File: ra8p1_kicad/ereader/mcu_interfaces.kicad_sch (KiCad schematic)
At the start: 8 parts, among them U1 R7KA8P1KFLCAC#UC0

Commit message: Wire e-reader user controls and record power architecture
Connect four protected page/volume inputs and power INT/KILL interfaces through the native hierarchy. Include exact sourcing, linked calculations, local symbols, expanded requirements, and a fresh eight-page PDF and full BOM.

Progress checkpoint, not fabrication release: power source, EN supervision and discharge remain unfinished. Configured ERC: 204 errors and 2 warnings, versus 208 and 2 at the previous checkpoint; six MCU disconnections resolved and two explicit power-draft gaps added. Page/volume sheet has zero findings. One independent review round: no findings. Arithmetic, netlist/BOM consistency and all PDF pages reviewed. Hardware-only hook bypass explicitly authorized.
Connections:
- net PAGE_PREV_N: now reaches U1.A12 (P309)
- net VOL_DOWN_N: now reaches U1.B12 (P311)
- net POWER_BUTTON_N: now reaches U1.B6 (P303)
- net PAGE_NEXT_N: now reaches U1.E10 (P310)
- net VOL_UP_N: now reaches U1.B14 (P909)
- net POWER_KILL_N: now reaches U1.D9 (P903)
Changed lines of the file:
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@@
 	(wire
 		(pts
+			(xy 264.16 76.2) (xy 279.4 76.2)
+		)
+		(stroke
+			(width 0)
+			(type default)
+		)
+	)
+	(wire
+		(pts
 			(xy 20.32 220.98) (xy 30.48 220.98)
 		)
@@
 	(wire
 		(pts
+			(xy 167.64 139.7) (xy 182.88 139.7)
+		)
+		(stroke
+			(width 0)
+			(type default)
+		)
+	)
+	(wire
+		(pts
+			(xy 264.16 55.88) (xy 279.4 55.88)
+		)
+		(stroke
+			(width 0)
+			(type default)
+		)
+	)
+	(wire
+		(pts
 			(xy 266.7 213.36) (xy 304.8 213.36)
 		)
@@
 	(wire
 		(pts
+			(xy 264.16 71.12) (xy 279.4 71.12)
+		)
+		(stroke
+			(width 0)
+			(type default)
+		)
+	)
+	(wire
+		(pts
 			(xy 71.12 124.46) (xy 96.52 124.46)
 		)
@@
 	(wire
 		(pts
+			(xy 167.64 124.46) (xy 182.88 124.46)
+		)
+		(stroke
+			(width 0)
+			(type default)
+		)
+	)
+	(wire
+		(pts
 			(xy 71.12 137.16) (xy 96.52 137.16)
 		)
@@
 	(wire
 		(pts
+			(xy 264.16 73.66) (xy 279.4 73.66)
+		)
+		(stroke
+			(width 0)
+			(type default)
+		)
+	)
+	(wire
+		(pts
 			(xy 71.12 121.92) (xy 96.52 121.92)
 		)
@@
 		)
 	)
+	(hierarchical_label "VOL_UP_N"
+		(shape input)
+		(at 182.88 139.7 0)
+		(effects
+			(font
+				(size 1.27 1.27)
+			)
+			(justify left)
+		)
+	)
 	(hierarchical_label "RADIO_DATA_READY"
 		(shape input)
@@
 		)
 	)
+	(hierarchical_label "POWER_BUTTON_N"
+		(shape input)
+		(at 279.4 55.88 0)
+		(effects
+			(font
+				(size 1.27 1.27)
+			)
+			(justify left)
+		)
+	)
+	(hierarchical_label "PAGE_PREV_N"
+		(shape input)
+		(at 279.4 71.12 0)
+		(effects
+			(font
+				(size 1.27 1.27)
+			)
+			(justify left)
+		)
+	)
+	(hierarchical_label "POWER_KILL_N"
+		(shape output)
+		(at 182.88 124.46 0)
+		(effects
+			(font
+				(size 1.27 1.27)
+			)
+			(justify left)
+		)
+	)
+	(hierarchical_label "VOL_DOWN_N"
+		(shape input)
+		(at 279.4 76.2 0)
+		(effects
+			(font
+				(size 1.27 1.27)
+			)
+			(justify left)
+		)
+	)
 	(hierarchical_label "RADIO_SCLK"
 		(shape output)
@@
 		)
 	)
+	(hierarchical_label "PAGE_NEXT_N"
+		(shape input)
+		(at 279.4 73.66 0)
+		(effects
+			(font
+				(size 1.27 1.27)
+			)
+			(justify left)
+		)
+	)
 	(symbol
 		(lib_id "power:+3V3")
@@
 		)
 		(pin "E10"
+			(alternate "P310_IN")
 		)
 		(pin "F14"
@@
 		)
 		(pin "B14"
+			(alternate "P909_IN")
 		)
 		(pin "C12"
 		)
 		(pin "D9"
+			(alternate "P903_OD")
 		)
 		(pin "D12"
@@
 		)
 		(pin "A12"
+			(alternate "P309_IN")
 		)
 		(pin "A17"
@@
 		)
 		(pin "B6"
+			(alternate "P303_IN")
 		)
 		(pin "B12"
+			(alternate "P311_IN")
 		)
 		(pin "B15"
@@
 		)
 		(pin "B6"
+			(alternate "P303_IN")
 		)
 		(pin "D10"
@@
 		)
 		(pin "A12"
+			(alternate "P309_IN")
 		)
 		(pin "E10"
+			(alternate "P310_IN")
 		)
 		(pin "B12"
+			(alternate "P311_IN")
 		)
 		(pin "C13"
@@
 		)
 		(pin "B14"
+			(alternate "P909_IN")
 		)
 		(pin "C12"
 		)
 		(pin "D9"
+			(alternate "P903_OD")
 		)
 		(pin "E11"
@@
 		)
 		(pin "D9"
+			(alternate "P903_OD")
 		)
 		(pin "J3"
@@
 		)
 		(pin "E10"
+			(alternate "P310_IN")
 		)
 		(pin "D11"
@@
 		)
 		(pin "A12"
+			(alternate "P309_IN")
 		)
 		(pin "A17"
@@
 		)
 		(pin "B6"
+			(alternate "P303_IN")
 		)
 		(pin "B12"
+			(alternate "P311_IN")
 		)
 		(pin "B15"
@@
 		)
 		(pin "B14"
+			(alternate "P909_IN")
 		)
 		(pin "C12"
@@
 		)
 		(pin "D9"
+			(alternate "P903_OD")
 		)
 		(pin "A16"
@@
 		)
 		(pin "B14"
+			(alternate "P909_IN")
 		)
 		(pin "E11"
@@
 		)
 		(pin "A12"
+			(alternate "P309_IN")
 		)
 		(pin "A17"
@@
 		)
 		(pin "B6"
+			(alternate "P303_IN")
 		)
 		(pin "B12"
+			(alternate "P311_IN")
 		)
 		(pin "B15"
@@
 		)
 		(pin "E10"
+			(alternate "P310_IN")
 		)
 		(pin "F14"
@@
 		)
 		(pin "A12"
+			(alternate "P309_IN")
 		)
 		(pin "A17"
@@
 		)
 		(pin "B6"
+			(alternate "P303_IN")
 		)
 		(pin "B12"
+			(alternate "P311_IN")
 		)
 		(pin "B15"
@@
 		)
 		(pin "E10"
+			(alternate "P310_IN")
 		)
 		(pin "F14"
@@
 		)
 		(pin "B14"
+			(alternate "P909_IN")
 		)
 		(pin "C12"
 		)
 		(pin "D9"
+			(alternate "P903_OD")
 		)
 		(pin "D12"
@@
 		)
 		(pin "B14"
+			(alternate "P909_IN")
 		)
 		(pin "C12"
@@
 		)
 		(pin "D9"
+			(alternate "P903_OD")
 		)
 		(pin "U5"
@@
 		)
 		(pin "A12"
+			(alternate "P309_IN")
 		)
 		(pin "A17"
@@
 		)
 		(pin "E10"
+			(alternate "P310_IN")
 		)
 		(pin "D11"
@@
 		)
 		(pin "B6"
+			(alternate "P303_IN")
 		)
 		(pin "B12"
+			(alternate "P311_IN")
 		)
 		(pin "C10"
@@
 		)
 		(pin "A12"
+			(alternate "P309_IN")
 		)
 		(pin "A5"
@@
 		)
 		(pin "D9"
+			(alternate "P903_OD")
 		)
 		(pin "C12"
 		)
 		(pin "B14"
+			(alternate "P909_IN")
 		)
 		(pin "B13"
@@
 		)
 		(pin "E10"
+			(alternate "P310_IN")
 		)
 		(pin "D11"
@@
 		)
 		(pin "B6"
+			(alternate "P303_IN")
 		)
 		(pin "B5"
@@
 		)
 		(pin "B12"
+			(alternate "P311_IN")
 		)
 		(pin "C11"
@@
 		)
 		(pin "B14"
+			(alternate "P909_IN")
 		)
 		(pin "C12"
 		)
 		(pin "D9"
+			(alternate "P903_OD")
 		)
 		(pin "D12"
@@
 		)
 		(pin "E10"
+			(alternate "P310_IN")
 		)
 		(pin "F14"
@@
 		)
 		(pin "A12"
+			(alternate "P309_IN")
 		)
 		(pin "A17"
@@
 		)
 		(pin "B6"
+			(alternate "P303_IN")
 		)
 		(pin "B12"
+			(alternate "P311_IN")
 		)
 		(pin "B15"

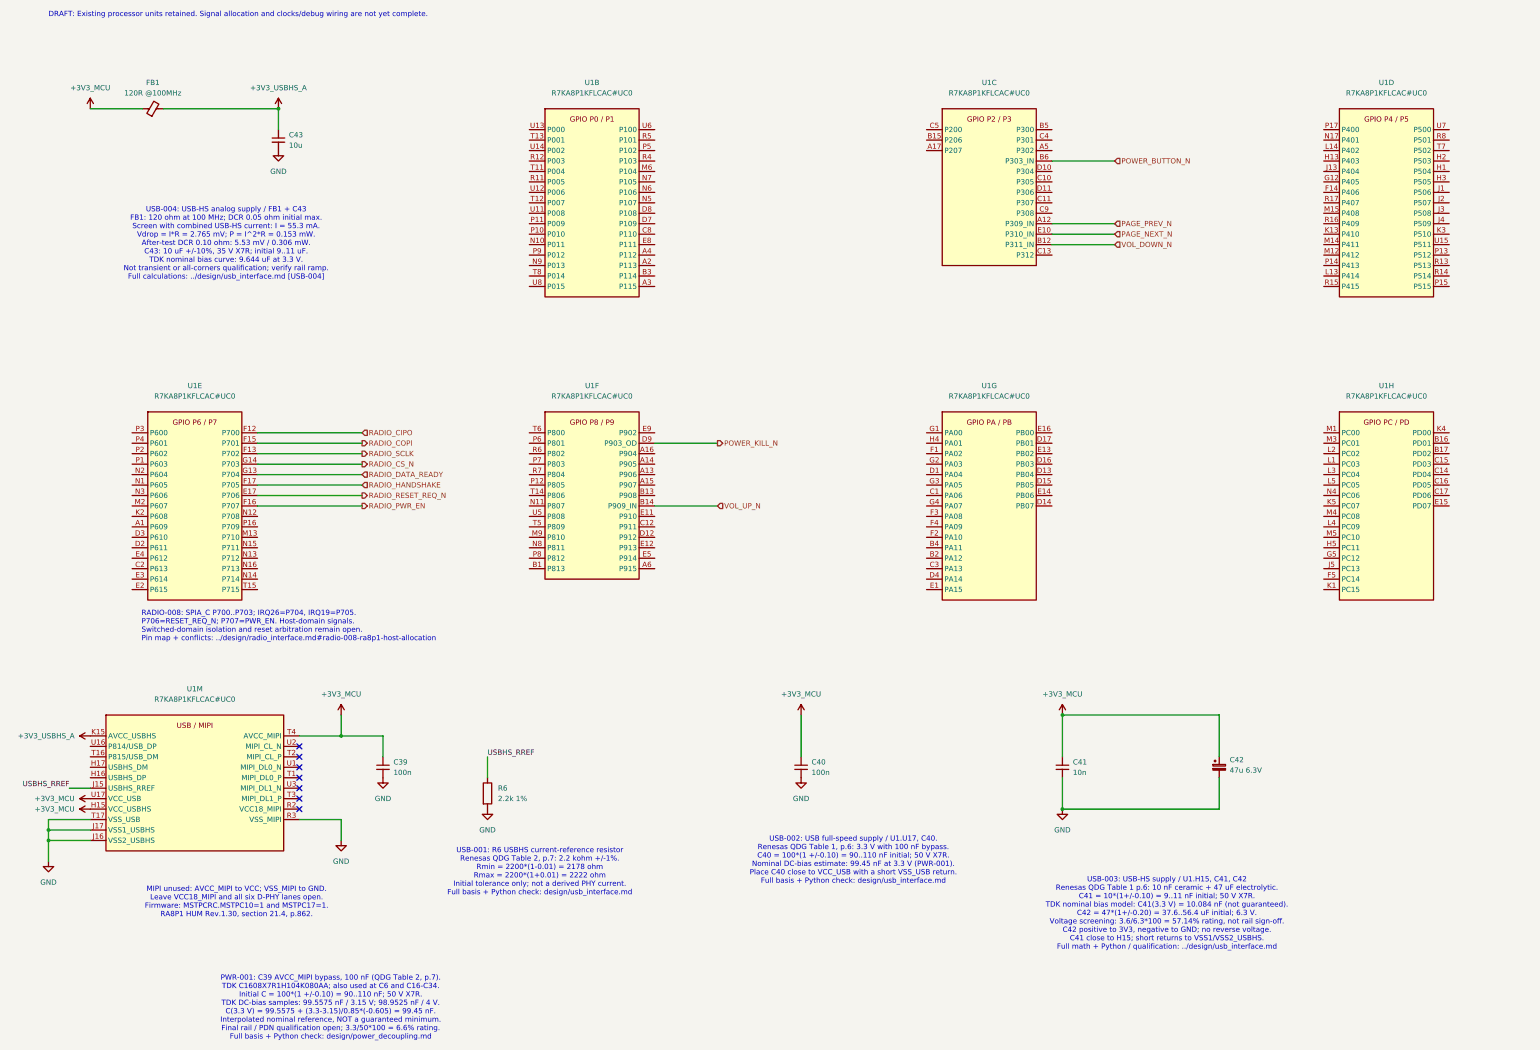
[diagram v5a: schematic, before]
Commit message: Connect SDRAM signals through the schematic hierarchy
Wire the verified 57-signal RA8P1 interface and separate source/load clock nets through R43. Refresh the native BOM, linked CMS-010 contract, and complete ten-page PDF.

ERC: 139 prior findings resolved, zero new identities; 145 errors and two active warnings remain in the unfinished design. MCU pin-role typing, command pullups, and timing qualification remain open under #827.
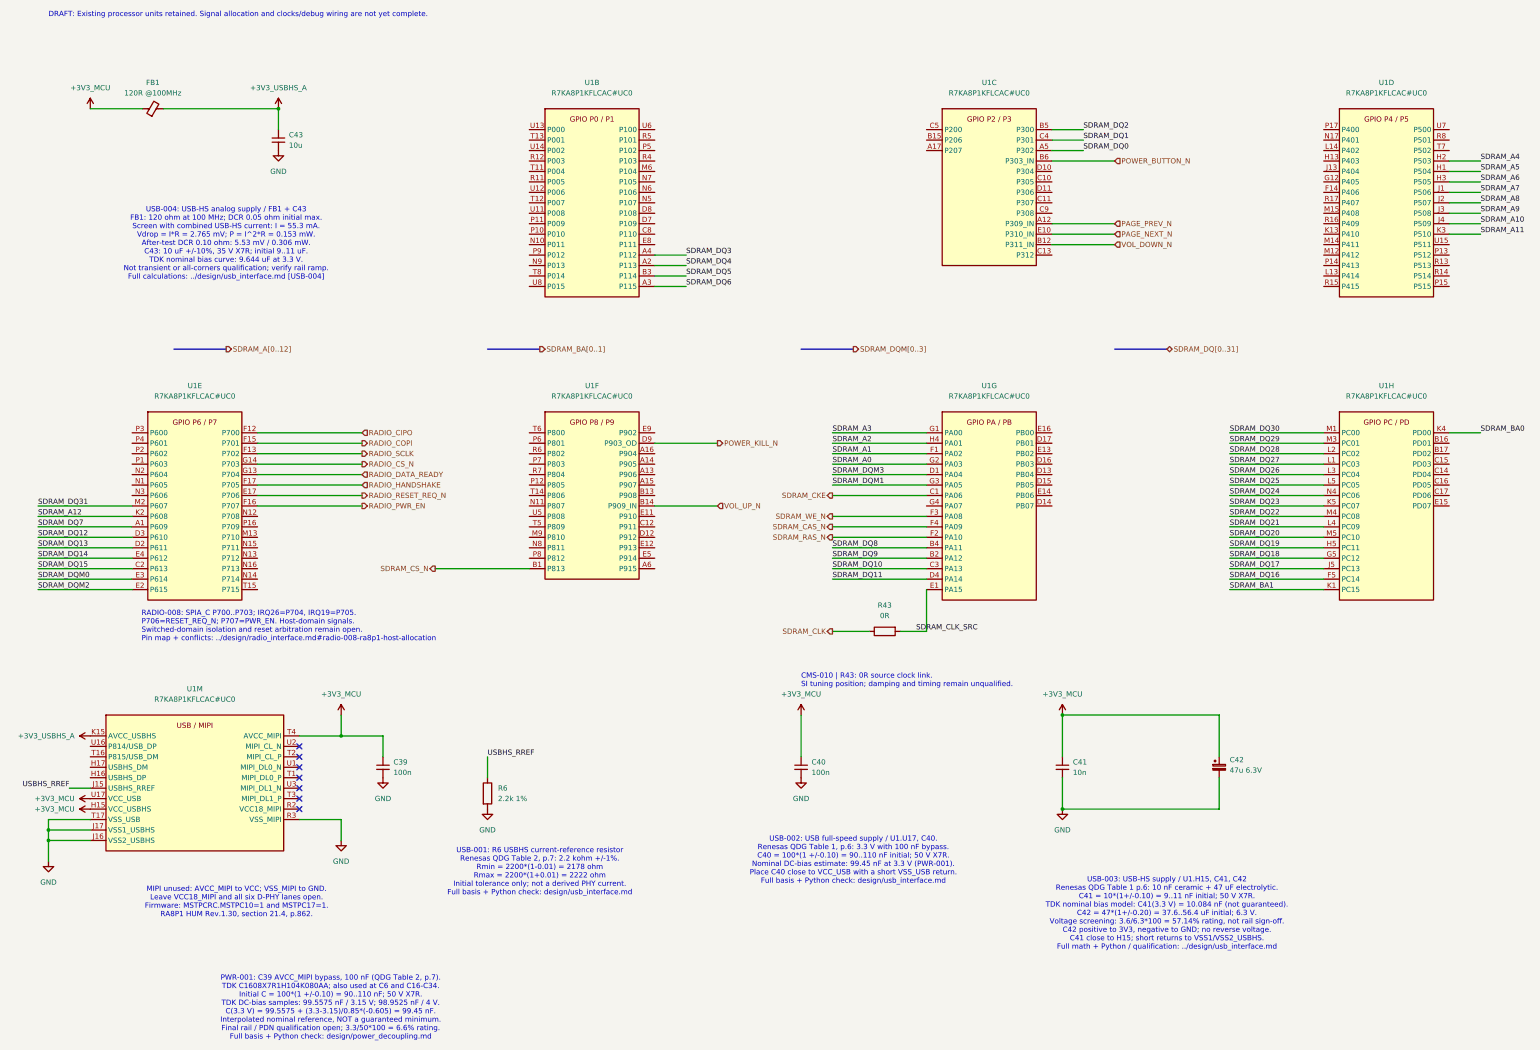
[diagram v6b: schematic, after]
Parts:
- added R43: 0R, symbol Device:R
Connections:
- net SDRAM_DQ7: now reaches U1.A1 (P609)
- net SDRAM_DQ15: now reaches U1.C2 (P613)
- net SDRAM_DQ13: now reaches U1.D2 (P611)
- net SDRAM_DQ12: now reaches U1.D3 (P610)
- net SDRAM_DQM2: now reaches U1.E2 (P615)
- net SDRAM_DQM0: now reaches U1.E3 (P614)
- net SDRAM_DQ14: now reaches U1.E4 (P612)
- net SDRAM_A12: now reaches U1.K2 (P608)
- net SDRAM_DQ31: now reaches U1.M2 (P607)
- net SDRAM_DQ0: now reaches U1.A5 (P302)
- net SDRAM_DQ2: now reaches U1.B5 (P300)
- net SDRAM_DQ1: now reaches U1.C4 (P301)
- net SDRAM_DQ9: now reaches U1.B2 (PA12)
- net SDRAM_DQ8: now reaches U1.B4 (PA11)
- net SDRAM_CKE: now reaches U1.C1 (PA06)
- net SDRAM_DQ10: now reaches U1.C3 (PA13)
- net SDRAM_DQM3: now reaches U1.D1 (PA04)
- net SDRAM_DQ11: now reaches U1.D4 (PA14)
- net SDRAM_CLK_SRC: now reaches U1.E1 (PA15)
- net SDRAM_CLK_SRC: now also R43.2
- net SDRAM_A1: now reaches U1.F1 (PA02)
- net SDRAM_RAS_N: now reaches U1.F2 (PA10)
- net SDRAM_WE_N: now reaches U1.F3 (PA08)
- net SDRAM_CAS_N: now reaches U1.F4 (PA09)
- net SDRAM_A3: now reaches U1.G1 (PA00)
- net SDRAM_A0: now reaches U1.G2 (PA03)
- net SDRAM_DQM1: now reaches U1.G3 (PA05)
- net SDRAM_A2: now reaches U1.H4 (PA01)
- net SDRAM_CS_N: now reaches U1.B1 (P813)
- net SDRAM_DQ4: now reaches U1.A2 (P113)
- net SDRAM_DQ6: now reaches U1.A3 (P115)
- net SDRAM_DQ3: now reaches U1.A4 (P112)
- net SDRAM_DQ5: now reaches U1.B3 (P114)
- net SDRAM_DQ16: now reaches U1.F5 (PC14)
- net SDRAM_DQ18: now reaches U1.G5 (PC12)
- net SDRAM_DQ19: now reaches U1.H5 (PC11)
- net SDRAM_DQ17: now reaches U1.J5 (PC13)
- net SDRAM_BA1: now reaches U1.K1 (PC15)
- net SDRAM_BA0: now reaches U1.K4 (PD00)
- net SDRAM_DQ23: now reaches U1.K5 (PC07)
- net SDRAM_DQ27: now reaches U1.L1 (PC03)
- net SDRAM_DQ28: now reaches U1.L2 (PC02)
- net SDRAM_DQ26: now reaches U1.L3 (PC04)
- net SDRAM_DQ21: now reaches U1.L4 (PC09)
- net SDRAM_DQ25: now reaches U1.L5 (PC05)
- net SDRAM_DQ30: now reaches U1.M1 (PC00)
- net SDRAM_DQ29: now reaches U1.M3 (PC01)
- net SDRAM_DQ22: now reaches U1.M4 (PC08)
- net SDRAM_DQ20: now reaches U1.M5 (PC10)
- net SDRAM_DQ24: now reaches U1.N4 (PC06)
- net SDRAM_A5: now reaches U1.H1 (P504)
- net SDRAM_A4: now reaches U1.H2 (P503)
- net SDRAM_A6: now reaches U1.H3 (P505)
- net SDRAM_A7: now reaches U1.J1 (P506)
- net SDRAM_A8: now reaches U1.J2 (P507)
- net SDRAM_A9: now reaches U1.J3 (P508)
- net SDRAM_A10: now reaches U1.J4 (P509)
- net SDRAM_A11: now reaches U1.K3 (P510)
- new net SDRAM_CLK: R43.1
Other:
- note added: "CMS-010 | R43: 0R source clock link. SI tuning position; damping and timing remain unqualified."
